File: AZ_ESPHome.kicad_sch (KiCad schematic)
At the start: 23 parts, among them U1 WeMos_D1_mini, U2 DHT11

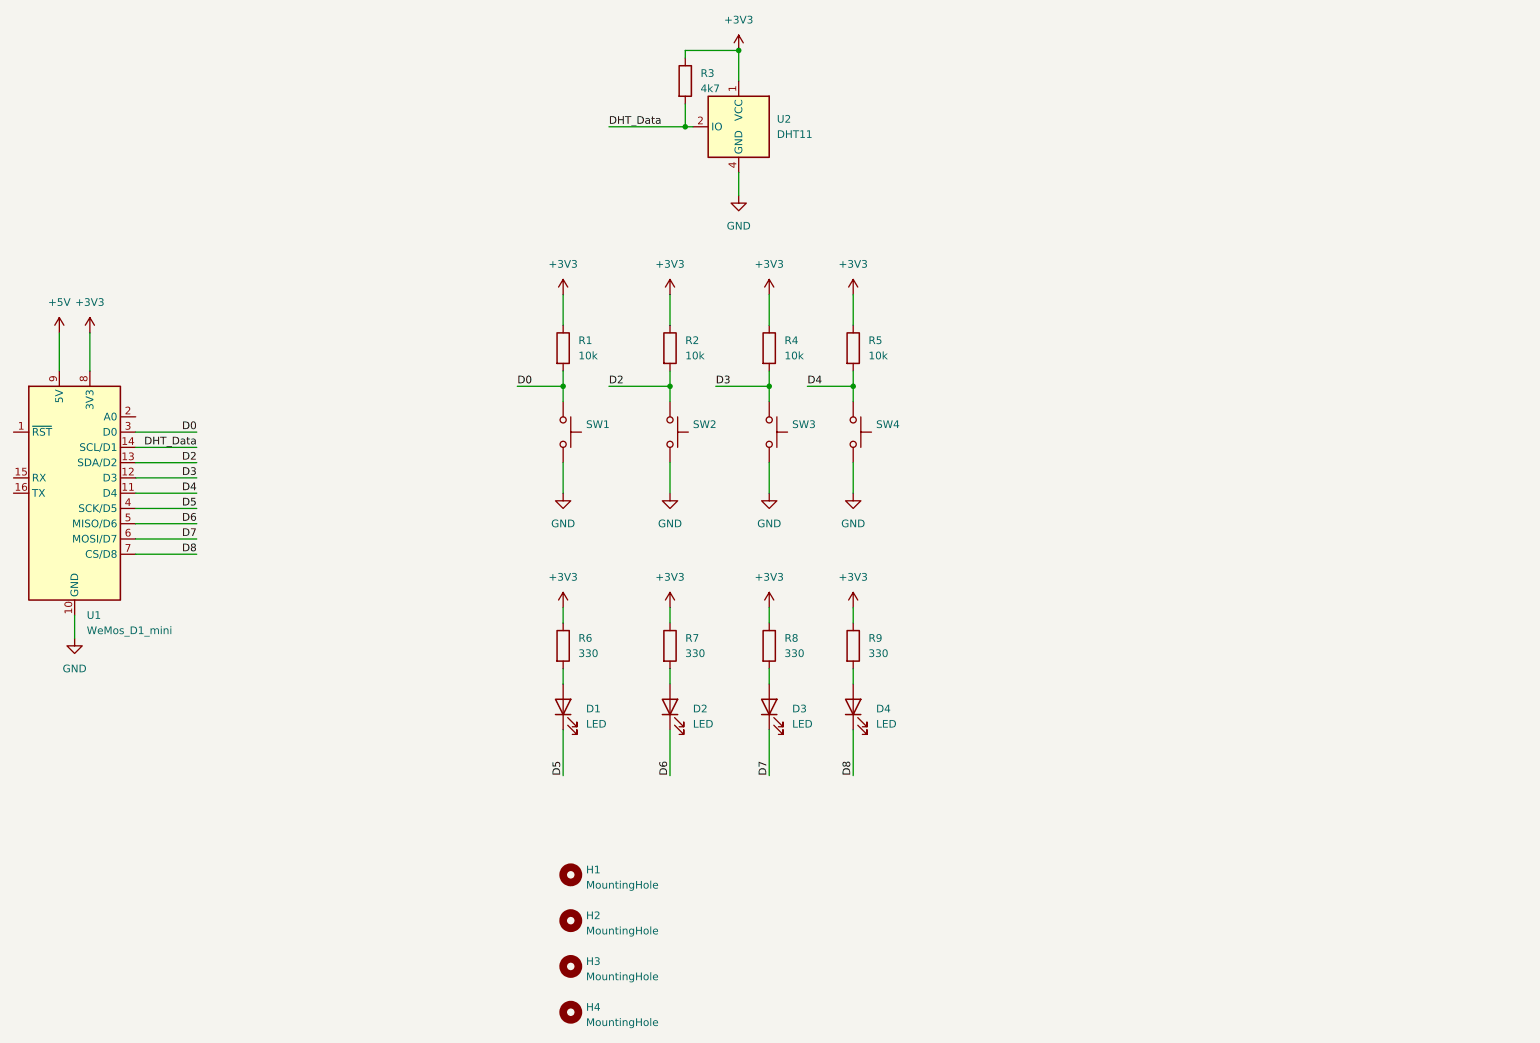
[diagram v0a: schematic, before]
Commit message: added Sch as PDF
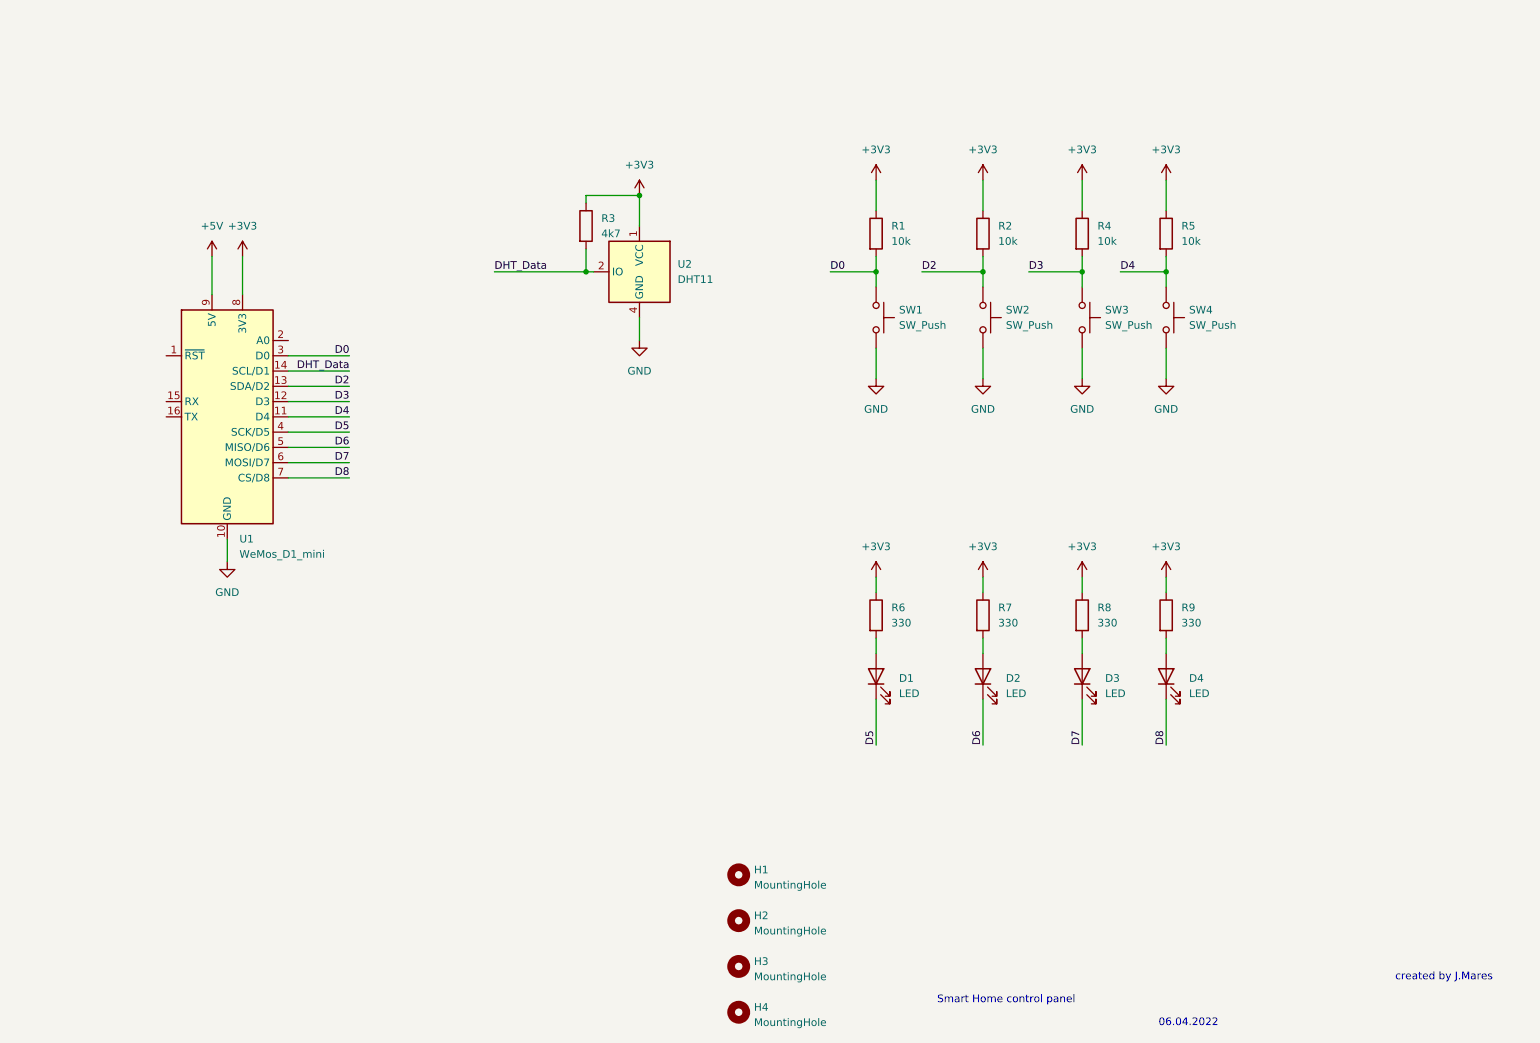
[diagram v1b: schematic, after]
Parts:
- SW1, SW2, SW3, SW4: value (none) -> SW_Push; footprint (none) -> Library_JM:SW_Push_1P1T_NO_6x6mm_H9.5mm
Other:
- note added: "${REVISION}"
- note added: "06.04.2022"
- note added: "Smart Home control panel"
- note added: "created by J.Mares"
- moved on the sheet: D1, D2, D3, D4, H1, H2, H3, H4, R1, R2, R3, R4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
